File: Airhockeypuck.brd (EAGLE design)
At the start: 80 x 80 mm, 24 parts, among them J1 USB-MB-H

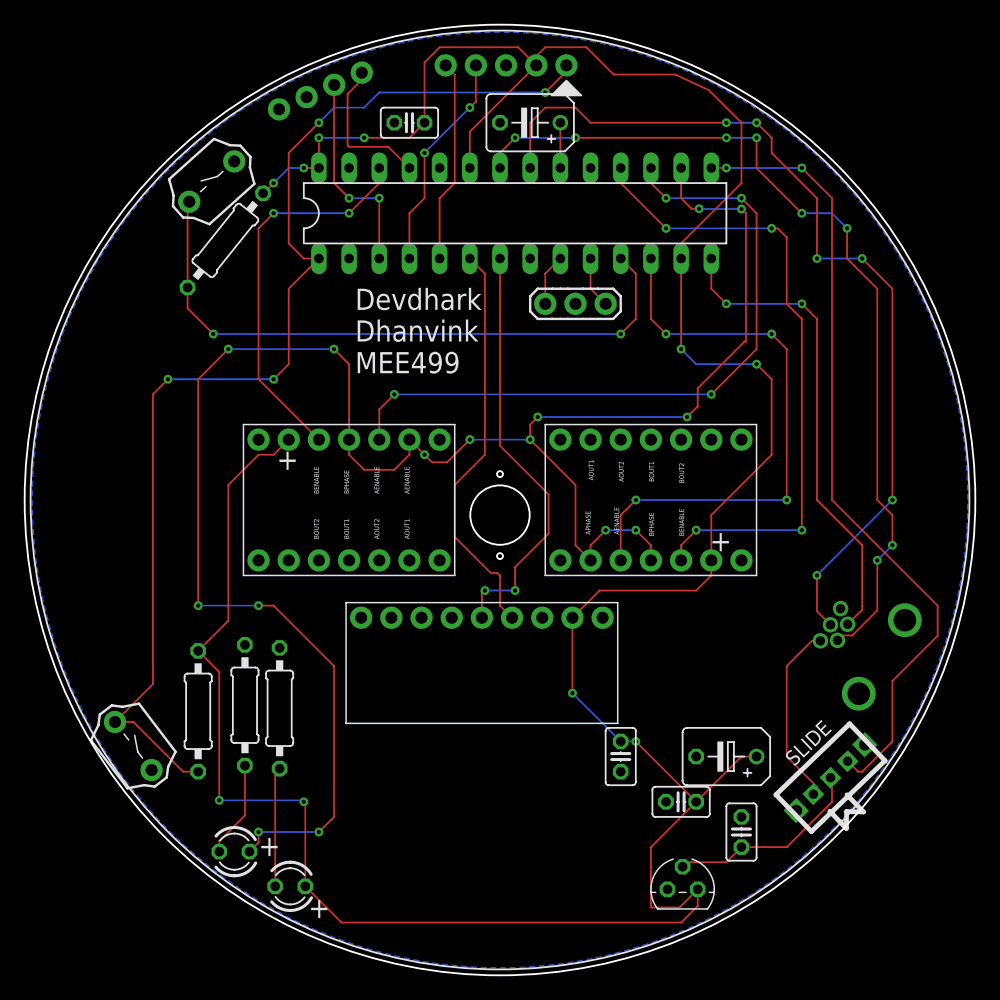
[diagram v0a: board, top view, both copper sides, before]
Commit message: Changed device DRV8835
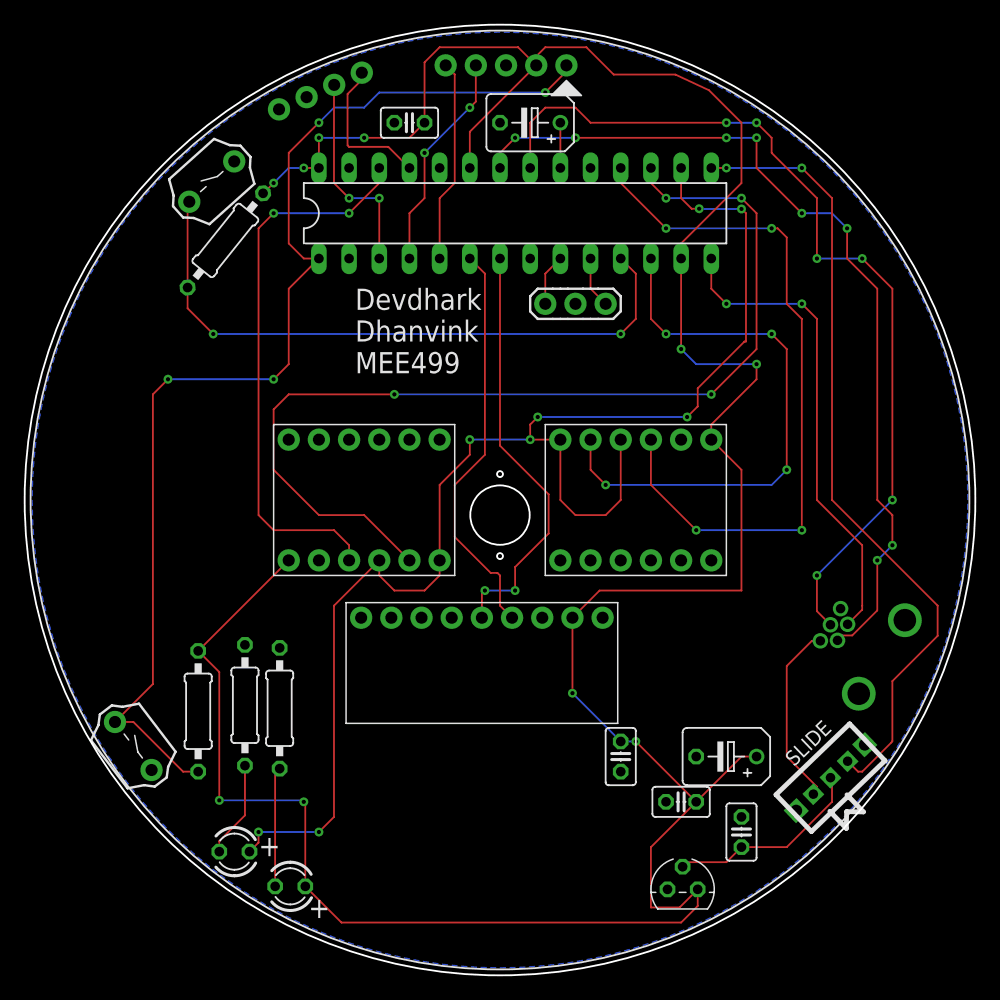
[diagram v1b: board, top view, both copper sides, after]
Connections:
- net +3V3: now also U$6.1.3.3V, U$7.1.3.3V; no longer U$6.9.VCC, U$7.9.VCC
- net A4: now also U$7.5.BIN1; no longer U$7.12.AENABLE
- net B15: now also U$6.3.AIN1; no longer U$6.10.BENABLE
- net B7: now also U$6.4.AIN2, U$6.6.BIN2, U$7.4.AIN2, U$7.6.BIN2; no longer U$6.11.BPHASE, U$6.13.APHASE, U$7.11.BPHASE, U$7.13.APHASE
- net B8: now also U$6.5.BIN1; no longer U$6.12.AENABLE
- net B9: now also U$7.3.AIN1; no longer U$7.10.BENABLE
- net GND: now also U$6.12.GND, U$7.12.GND; no longer U$6.8.GND, U$7.8.GND
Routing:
- net B7: track 158.6 -> 118.3 mm, vias 15 -> 8
- net B8: track 59.0 -> 85.1 mm
- net B15: track 32.9 -> 47.1 mm
- net +3V3: track 254.3 -> 246.6 mm
- net B9: track 54.3 -> 60.4 mm
- net A4: track 48.6 -> 47.8 mm
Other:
- board text removed: "AENABLE"
- board text removed: "AOUT1"
- board text removed: "AOUT2"
- board text removed: "APHASE"
- board text removed: "BENABLE"
- board text removed: "BOUT1"
- board text removed: "BOUT2"
- board text removed: "BPHASE"
